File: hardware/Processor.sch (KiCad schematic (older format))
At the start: 25 parts, among them IC1 74HC00, IC10 W65C22, IC2 W65C02, IC3 74HC138, IC4 SYSTEM ROM, IC5 RAM, IC6 W65C22, IC7 W65C51

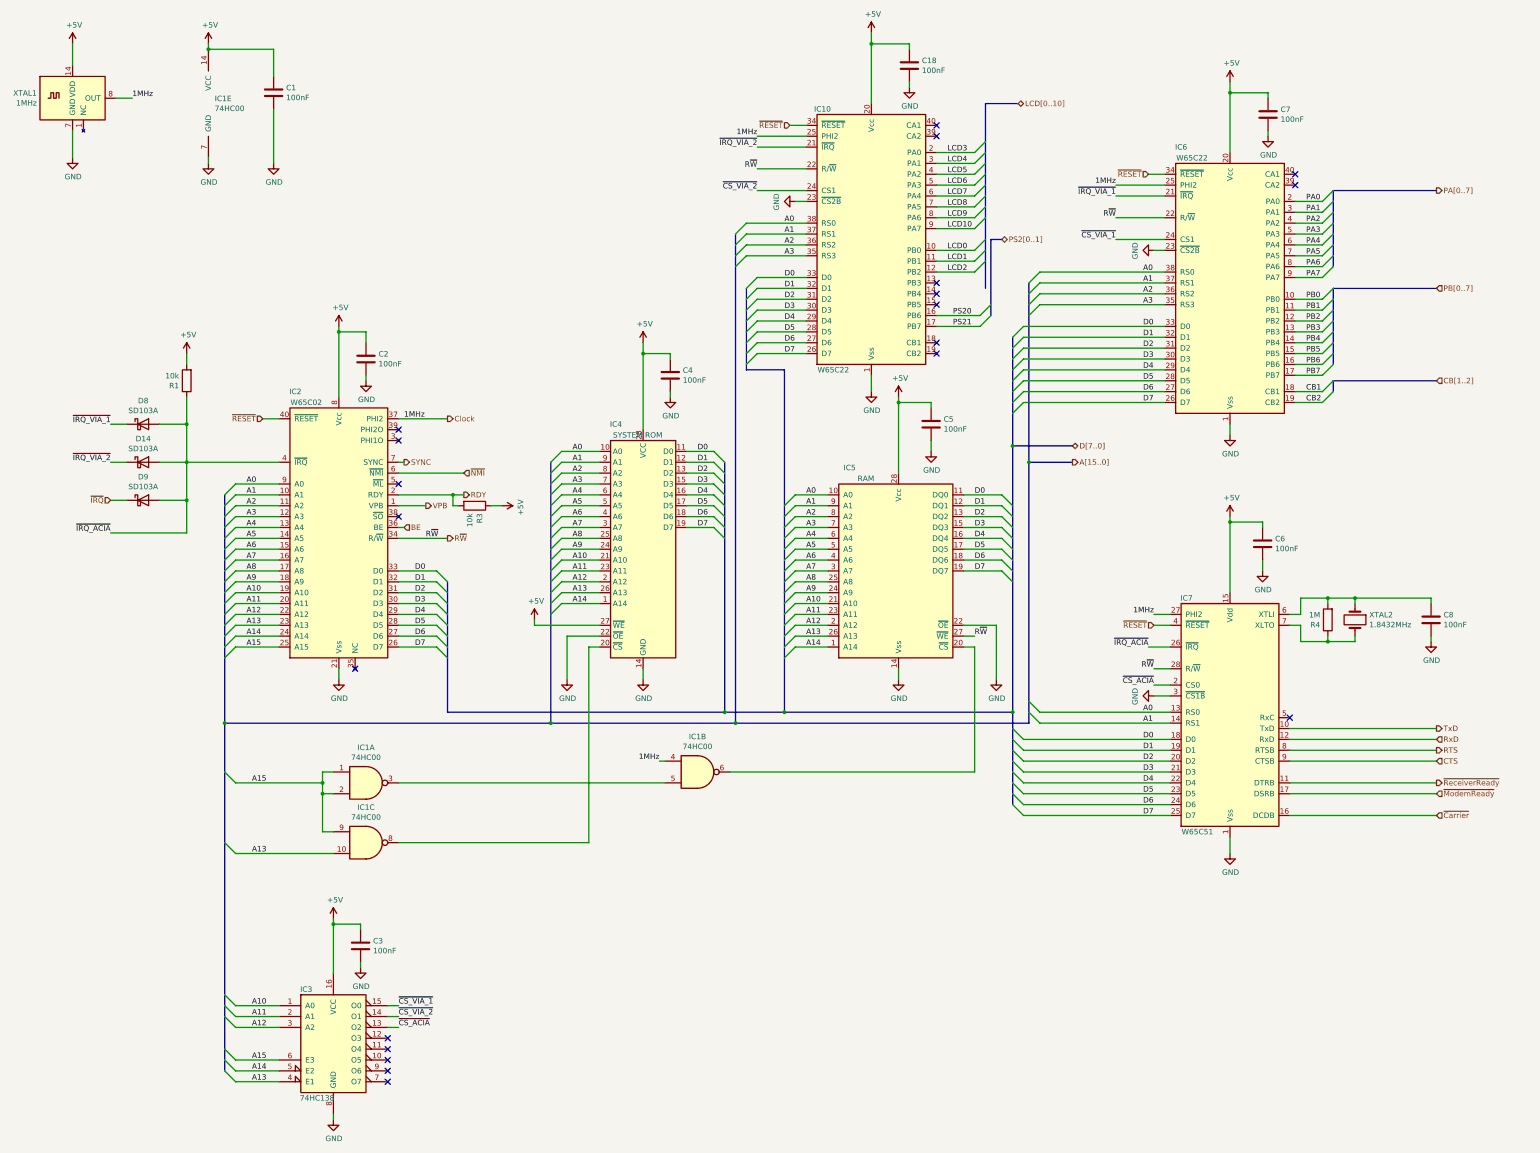
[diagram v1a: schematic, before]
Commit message: Finalize schematic and layout. Add switch for carrier detect
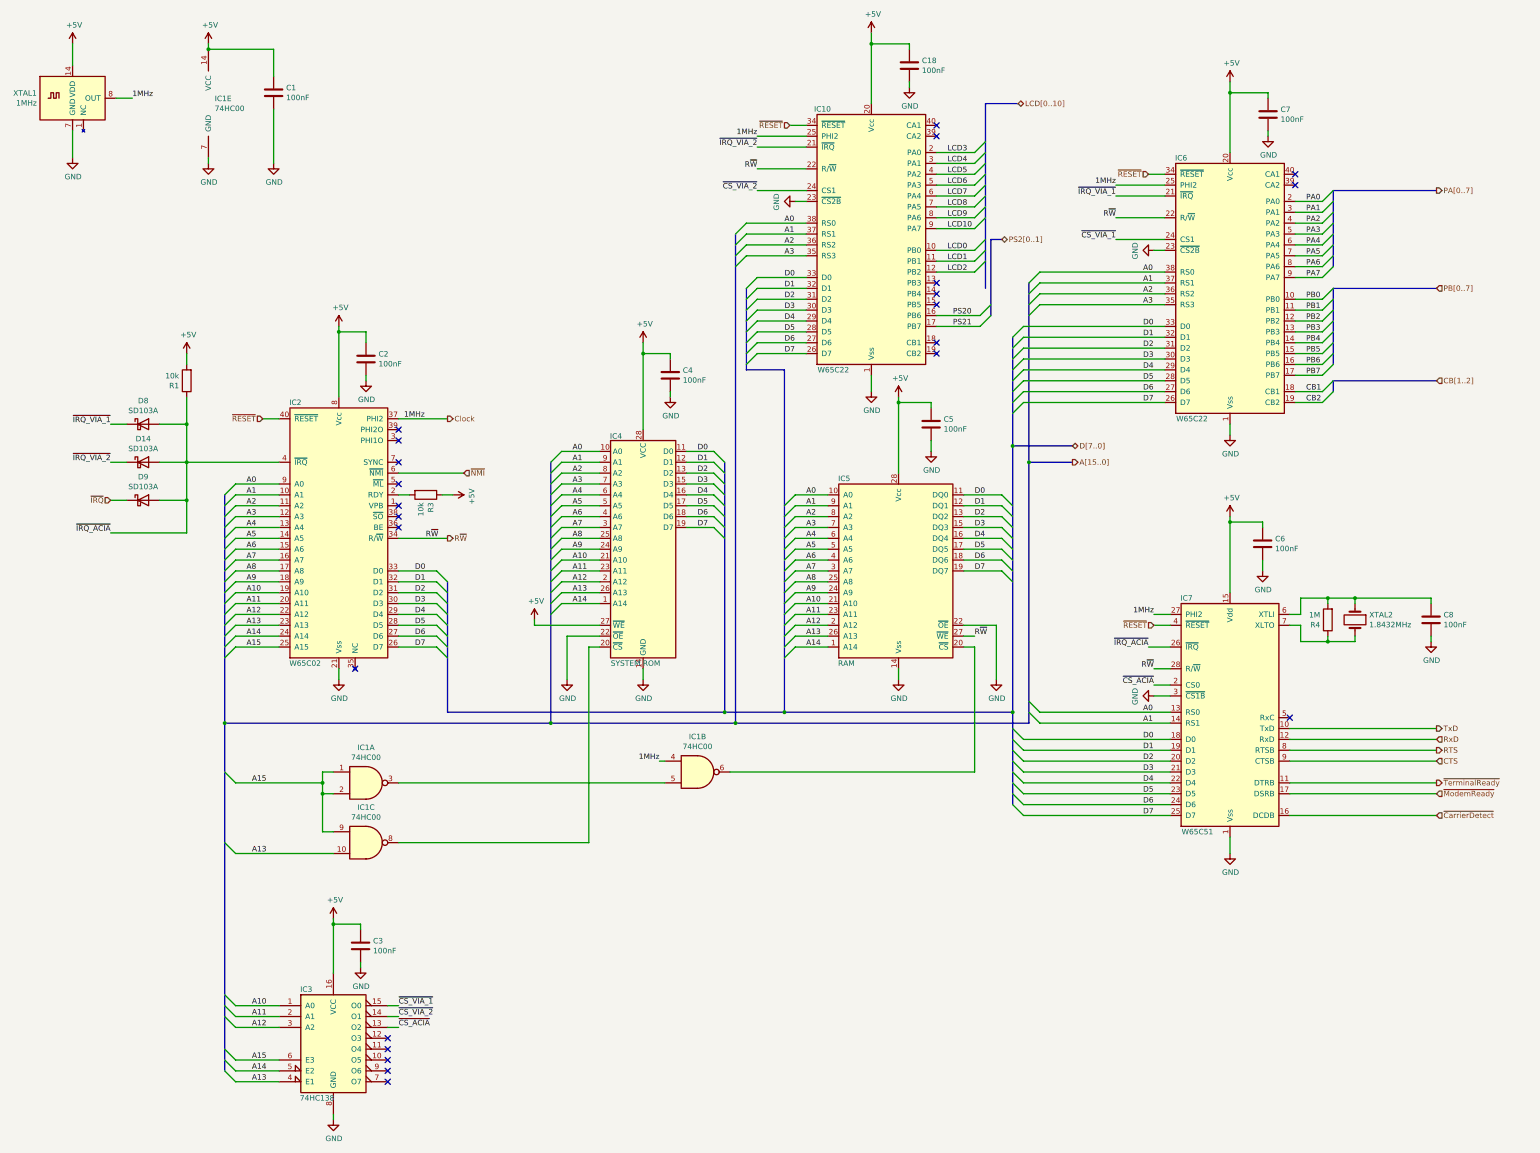
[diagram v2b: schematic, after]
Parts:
- IC4: Mfr. Aries Electronics -> Microchip Technology / Atmel; Mfr. No. 28-6553-10* -> AT28C256-15PU; Mouser 535-28-6553-10 -> 556-AT28C256-15PU
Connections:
- net BE: no longer names the net of IC2.36 (BE)
- net RDY: no longer names the net of IC2.2 (RDY), R3.2
- net SYNC: no longer names the net of IC2.7 (SYNC)
- net VPB: no longer names the net of IC2.1 (VPB)
- net ~Carrier renamed ~CarrierDetect
- net ~ReceiverReady renamed ~TerminalReady
- no-connect marks 20 -> 23
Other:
- moved on the sheet: R3
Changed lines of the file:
@@
 Date "2019-10-08"
 Rev "1.0"
-Comp ""
+Comp "https://www.kampis-elektroecke.de"
 Comment1 "Author: Daniel Kampert"
 Comment2 ""
@@
 AR Path="/5EBEAF78" Ref="IC?"  Part="1"
 AR Path="/5EB09E21/5EBEAF78" Ref="IC2"  Part="1"
-F 0 "IC2" H 3400 6650 50  0000 C CNN
-F 1 "W65C02" H 3500 6550 50  0000 C CNN
+F 0 "IC2" H 3400 6550 50  0000 C CNN
+F 1 "W65C02" H 3490 4150 50  0000 C CNN
 F 2 "Package_DIP:DIP-40_W15.24mm_LongPads" H 3800 5050 50  0001 C CNN
 F 3 "https://www.westerndesigncenter.com/wdc/documentation/w65c02s.pdf" H 3800 5350 50  0001 C CNN
@@
 L Device:R R?
 U 1 1 5EBEB08E
-P 5050 5100
+P 4600 5000
 AR Path="/5EBEB08E" Ref="R?"  Part="1"
 AR Path="/5EB09E21/5EBEB08E" Ref="R3"  Part="1"
-F 0 "R3" H 5120 5146 50  0000 L CNN
-F 1 "10k" H 5120 5055 50  0000 L CNN
-F 2 "Resistor_THT:R_Axial_DIN0207_L6.3mm_D2.5mm_P7.62mm_Horizontal" V 4980 5100 50  0001 C CNN
-F 3 "https://www.mouser.de/datasheet/2/447/Yageo%20LR_MFP_2013-594635.pdf" H 5050 5100 50  0001 C CNN
-F 4 "Yageo" H 5050 5100 50  0001 C CNN "Mfr."
-F 5 "MFP-25BRD52-10K" H 5050 5100 50  0001 C CNN "Mfr. No."
-F 6 "603-MFP-25BRD52-10K" H 5050 5100 50  0001 C CNN "Mouser"
-	1    5050 5100
+F 0 "R3" H 4670 5046 50  0000 L CNN
+F 1 "10k" H 4670 4955 50  0000 L CNN
+F 2 "Resistor_THT:R_Axial_DIN0207_L6.3mm_D2.5mm_P7.62mm_Horizontal" V 4530 5000 50  0001 C CNN
+F 3 "https://www.mouser.de/datasheet/2/447/Yageo%20LR_MFP_2013-594635.pdf" H 4600 5000 50  0001 C CNN
+F 4 "Yageo" H 4600 5000 50  0001 C CNN "Mfr."
+F 5 "MFP-25BRD52-10K" H 4600 5000 50  0001 C CNN "Mfr. No."
+F 6 "603-MFP-25BRD52-10K" H 4600 5000 50  0001 C CNN "Mouser"
+	1    4600 5000
 	0    1    1    0
 $EndComp
-Wire Wire Line
-	4850 5100 4850 5000
 NoConn ~ 4350 4900
 Wire Wire Line
-	4350 5300 4400 5300
-Wire Wire Line
-	4350 5100 4600 5100
-Wire Wire Line
-	4350 5000 4850 5000
+	4350 5000 4450 5000
 Wire Wire Line
 	2850 4900 3250 4900
@@
 Text Label 4500 6400 0    50   ~ 0
 D7
-Wire Wire Line
-	4900 5100 4850 5100
-Wire Wire Line
-	4850 5000 4950 5000
-Connection ~ 4850 5000
-Wire Wire Line
-	4350 4700 4400 4700
 Connection ~ 2750 7100
 Wire Wire Line
@@
 AR Path="/5EBEAF7E" Ref="IC?"  Part="1"
 AR Path="/5EB09E21/5EBEAF7E" Ref="IC6"  Part="1"
-F 0 "IC6" H 11550 4400 50  0000 C CNN
-F 1 "W65C22" H 11650 4300 50  0000 C CNN
+F 0 "IC6" H 11550 4300 50  0000 C CNN
+F 1 "W65C22" H 11650 1900 50  0000 C CNN
 F 2 "Package_DIP:DIP-40_W15.24mm_LongPads" H 12000 3100 50  0001 C CNN
 F 3 "https://www.westerndesigncenter.com/wdc/documentation/w65c22s.pdf" H 12000 3100 50  0001 C CNN
@@
 AR Path="/5EBEAF84" Ref="IC?"  Part="1"
 AR Path="/5EB09E21/5EBEAF84" Ref="IC5"  Part="1"
-F 0 "IC5" H 8500 6650 50  0000 C CNN
-F 1 "RAM" H 8650 6550 50  0000 C CNN
+F 0 "IC5" H 8450 6550 50  0000 C CNN
+F 1 "RAM" H 8470 4850 50  0000 C CNN
 F 2 "Package_DIP:DIP-28_W15.24mm_LongPads" H 8950 5700 50  0001 C CNN
 F 3 "https://www.alliancememory.com/wp-content/uploads/pdf/AS6C62256A.pdf" H 8950 5700 50  0001 C CNN
@@
 	7000 4600 7250 4600
 Wire Wire Line
-	5200 5100 5300 5100
+	4750 5000 4850 5000
 $Comp
 L power:+5V #PWR?
 U 1 1 5EBEB095
-P 5300 5100
+P 4850 5000
 AR Path="/5EBEB095" Ref="#PWR?"  Part="1"
 AR Path="/5EB09E21/5EBEB095" Ref="#PWR014"  Part="1"
-F 0 "#PWR014" H 5300 4950 50  0001 C CNN
-F 1 "+5V" H 5315 5273 50  0000 C CNN
-F 2 "" H 5300 5100 50  0001 C CNN
-F 3 "" H 5300 5100 50  0001 C CNN
-	1    5300 5100
+F 0 "#PWR014" H 4850 4850 50  0001 C CNN
+F 1 "+5V" H 4865 5173 50  0000 C CNN
+F 2 "" H 4850 5000 50  0001 C CNN
+F 3 "" H 4850 5000 50  0001 C CNN
+	1    4850 5000
 	0    1    1    0
 $EndComp
@@
 Text Label 10950 2650 2    50   ~ 0
 ~CS_VIA_1
-Text HLabel 4950 5000 2    50   Output ~ 0
-RDY
 Text HLabel 4950 4800 2    50   Input ~ 0
 ~NMI
-Text HLabel 4400 4700 2    50   Output ~ 0
-SYNC
-Text HLabel 4600 5100 2    50   Output ~ 0
-VPB
-Text HLabel 4400 5300 2    50   Input ~ 0
-BE
 Text Label 10950 2250 2    50   ~ 0
 ~IRQ_VIA_1
@@
 Wire Wire Line
 	4350 7650 6800 7650
-$Comp
-L Memory_EEPROM:28C256 IC?
-U 1 1 5EBEAFAB
-P 6600 5500
-AR Path="/5EBEAFAB" Ref="IC?"  Part="1"
-AR Path="/5EB09E21/5EBEAFAB" Ref="IC4"  Part="1"
-F 0 "IC4" H 6350 6650 50  0000 C CNN
-F 1 "SYSTEM ROM" H 6550 6550 50  0000 C CNN
-F 2 "Package_DIP:DIP-28_W15.24mm_LongPads" H 6600 5500 50  0001 C CNN
-F 3 "http://ww1.microchip.com/downloads/en/DeviceDoc/doc0006.pdf" H 6600 5500 50  0001 C CNN
-F 4 "Aries Electronics" H 6600 5500 50  0001 C CNN "Mfr."
-F 5 "28-6553-10*" H 6600 5500 50  0001 C CNN "Mfr. No."
-F 6 "535-28-6553-10" H 6600 5500 50  0001 C CNN "Mouser"
-	1    6600 5500
-	1    0    0    -1
-$EndComp
 Text HLabel 9900 2650 2    50   BiDi ~ 0
 PS2[0..1]
@@
 	12550 7650 13900 7650
 Text HLabel 13900 7650 2    50   Output ~ 0
-~ReceiverReady
+~TerminalReady
 Text HLabel 13900 7950 2    50   Input ~ 0
-~Carrier
+~CarrierDetect
 Wire Wire Line
 	12550 7950 13900 7950
@@
 NoConn ~ 9300 1600
 NoConn ~ 9300 1700
-Wire Bus Line
-	9800 2650 9800 3350
-Wire Bus Line
-	10150 4700 10150 7100
-Wire Bus Line
-	7450 2600 7450 7100
-Wire Bus Line
-	10150 3050 10150 4700
-Wire Bus Line
-	12950 3100 12950 3800
-Wire Bus Line
-	12950 2200 12950 2900
-Wire Bus Line
-	7350 4700 7350 7000
-Wire Bus Line
-	2750 7100 2750 10300
-Wire Bus Line
-	9750 1400 9750 3100
-Wire Bus Line
-	7550 3100 7550 3850
-Wire Bus Line
-	10000 7000 10000 7850
-Wire Bus Line
-	10000 3550 10000 4550
-Wire Bus Line
-	4800 5800 4800 7000
-Wire Bus Line
-	2750 5000 2750 7100
-Wire Bus Line
-	10000 4550 10000 7000
-Wire Bus Line
-	7900 3850 7900 7000
-Wire Bus Line
-	5750 4700 5750 7100
 Text HLabel 4800 4300 2    50   Output ~ 0
 Clock
+$Comp
+L Memory_EEPROM:28C256 IC?
+U 1 1 5EBEAFAB
+P 6600 5500
+AR Path="/5EBEAFAB" Ref="IC?"  Part="1"
+AR Path="/5EB09E21/5EBEAFAB" Ref="IC4"  Part="1"
+F 0 "IC4" H 6350 6540 50  0000 C CNN
+F 1 "SYSTEM ROM" H 6530 4450 50  0000 C CNN
+F 2 "Package_DIP:DIP-28_W15.24mm_LongPads" H 6600 5500 50  0001 C CNN
+F 3 "http://ww1.microchip.com/downloads/en/DeviceDoc/doc0006.pdf" H 6600 5500 50  0001 C CNN
+F 4 "Microchip Technology / Atmel" H 6600 5500 50  0001 C CNN "Mfr."
+F 5 "AT28C256-15PU" H 6600 5500 50  0001 C CNN "Mfr. No."
+F 6 "556-AT28C256-15PU" H 6600 5500 50  0001 C CNN "Mouser"
+	1    6600 5500
+	1    0    0    -1
+$EndComp
+NoConn ~ 4350 5300
+NoConn ~ 4350 5100
+NoConn ~ 4350 4700
+Wire Bus Line
+	9800 2650 9800 3350
+Wire Bus Line
+	10150 4700 10150 7100
+Wire Bus Line
+	7450 2600 7450 7100
+Wire Bus Line
+	10150 3050 10150 4700
+Wire Bus Line
+	12950 3100 12950 3800
+Wire Bus Line
+	12950 2200 12950 2900
+Wire Bus Line
+	7350 4700 7350 7000
+Wire Bus Line
+	2750 7100 2750 10300
+Wire Bus Line
+	9750 1400 9750 3100
+Wire Bus Line
+	7550 3100 7550 3850
+Wire Bus Line
+	10000 7000 10000 7850
+Wire Bus Line
+	10000 3550 10000 4550
+Wire Bus Line
+	4800 5800 4800 7000
+Wire Bus Line
+	2750 5000 2750 7100
+Wire Bus Line
+	10000 4550 10000 7000
+Wire Bus Line
+	7900 3850 7900 7000
+Wire Bus Line
+	5750 4700 5750 7100
 $EndSCHEMATC
